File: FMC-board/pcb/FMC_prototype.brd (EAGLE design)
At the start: 76.5 x 69 mm, 111 parts, among them Q1 SSM3J328R, U1 4901, U2 7933, U3 ADN4663, U4 ADN4663, U5 ADN4664, U6 PDS1, U7 4901, U8 FMC_SINGLE_WIDTH_MODULE

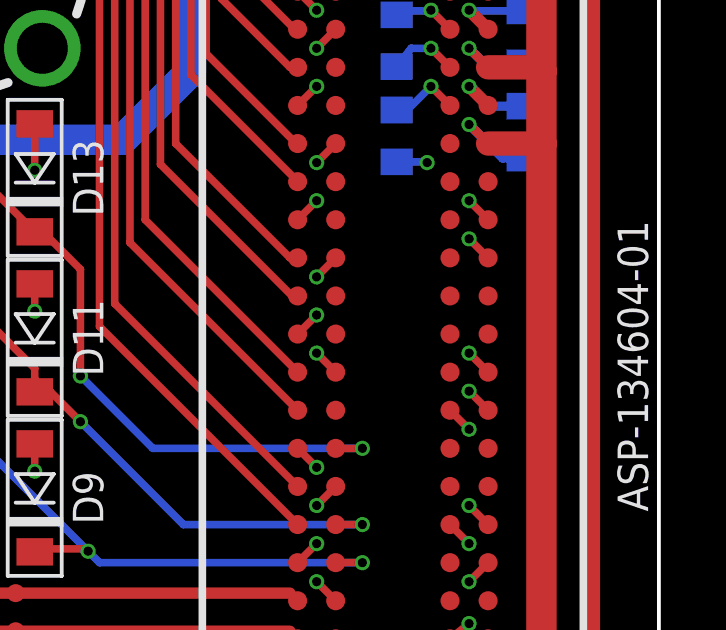
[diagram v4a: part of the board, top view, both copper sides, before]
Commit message: Tied the TDI/TDO pins together on the FMC header.
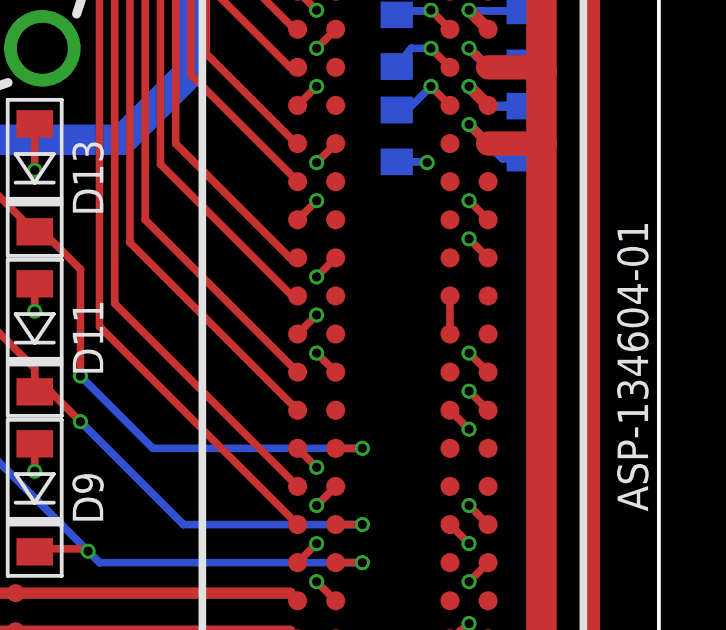
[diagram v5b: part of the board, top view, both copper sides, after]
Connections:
- new net TDI-TDO: FMC.P$110, FMC.P$111
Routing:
- net TDI-TDO: track 0.00 -> 1.27 mm
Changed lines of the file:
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@@
 <wire x1="-61.214" y1="21.082" x2="-56.4896" y2="21.082" width="0.254" layer="16"/>
+</signal>
+<signal name="TDI-TDO">
+<contactref element="FMC" pad="P$110"/>
+<contactref element="FMC" pad="P$111"/>
+<wire x1="3.937" y1="44.831" x2="3.937" y2="43.561" width="0.254" layer="1"/>
 </signal>
 </signals>
